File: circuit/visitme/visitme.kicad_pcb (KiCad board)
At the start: 2 copper layers, 16 parts, among them J5V1 Conn_01x01_Female, Q1 BC237

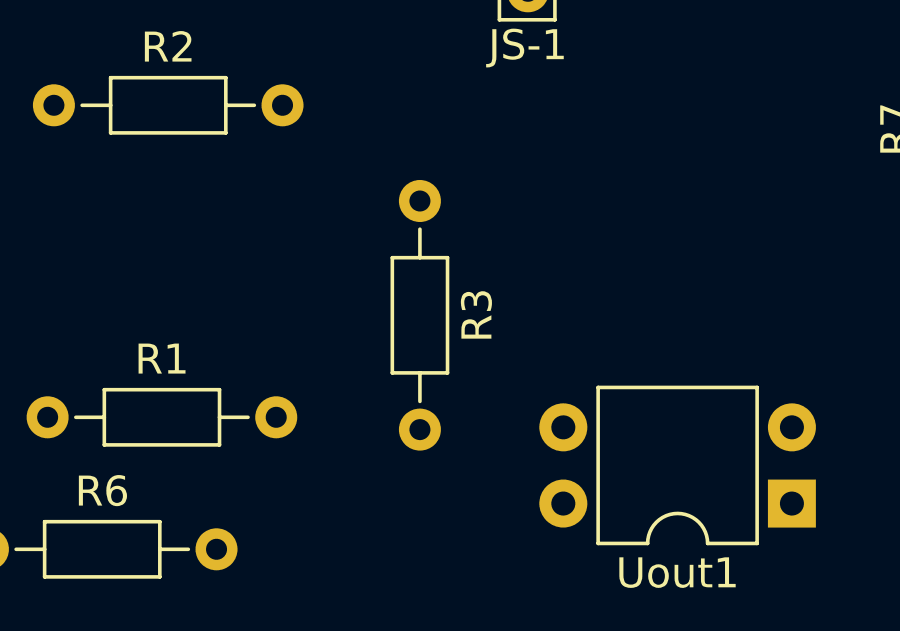
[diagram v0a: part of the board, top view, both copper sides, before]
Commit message: removed redundant 470k
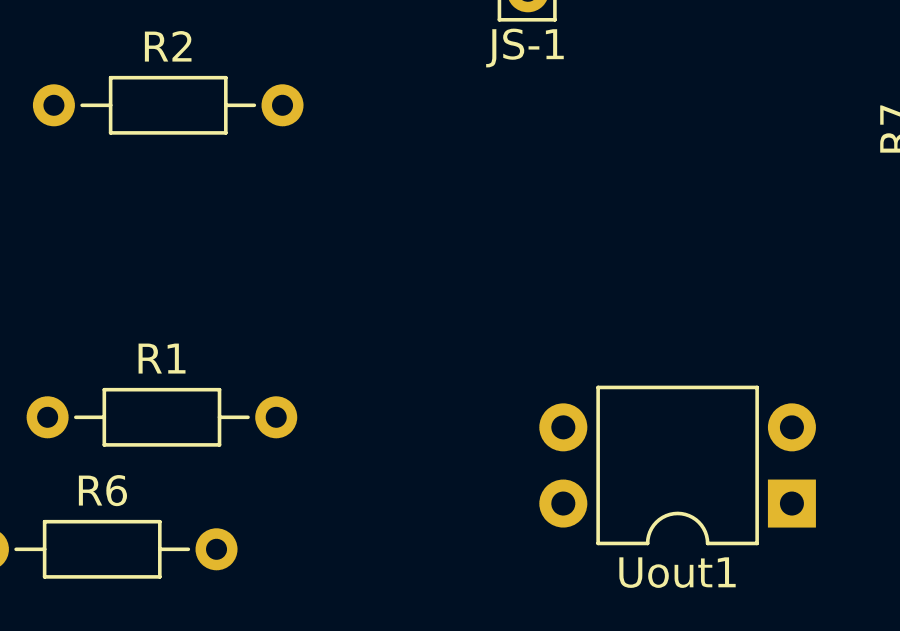
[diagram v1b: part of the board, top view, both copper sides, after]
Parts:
- removed R3: 470k, Resistor_THT:R_Axial_DIN0204_L3.6mm_D1.6mm_P7.62mm_Horizontal
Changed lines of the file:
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@@
   )
   (net 0 "")
-  (net 1 "Net-(Q1-Pad1)")
+  (net 1 "Net-(Q1-C)")
   (net 2 "D6 Data Out")
   (net 3 "+5V")
@@
     (property "Sheetfile" "visitme.kicad_sch")
     (property "Sheetname" "")
+    (property "ki_description" "Generic connector, single row, 01x01, script generated (kicad-library-utils/schlib/autogen/connector/)")
+    (property "ki_keywords" "connector")
     (attr through_hole)
     (fp_text reference "JGND1" (at 0 1.8) (layer "F.SilkS")
@@
     (property "Sheetfile" "visitme.kicad_sch")
     (property "Sheetname" "")
+    (property "ki_description" "Generic connector, single row, 01x01, script generated (kicad-library-utils/schlib/autogen/connector/)")
+    (property "ki_keywords" "connector")
     (attr through_hole)
     (fp_text reference "JS-1" (at 0 1.8) (layer "F.SilkS")
@@
     (property "Sheetfile" "visitme.kicad_sch")
     (property "Sheetname" "")
+    (property "ki_description" "Generic connector, single row, 01x01, script generated (kicad-library-utils/schlib/autogen/connector/)")
+    (property "ki_keywords" "connector")
     (attr through_hole)
     (fp_text reference "JDO1" (at 0 1.8) (layer "F.SilkS")
@@
     (property "Sheetfile" "visitme.kicad_sch")
     (property "Sheetname" "")
+    (property "ki_description" "Resistor")
+    (property "ki_keywords" "R res resistor")
     (attr through_hole)
     (fp_text reference "R4" (at 3.81 -1.92) (layer "F.SilkS")
@@
     (property "Sheetfile" "visitme.kicad_sch")
     (property "Sheetname" "")
+    (property "ki_description" "Generic connector, single row, 01x01, script generated (kicad-library-utils/schlib/autogen/connector/)")
+    (property "ki_keywords" "connector")
     (attr through_hole)
     (fp_text reference "JDI1" (at 0 1.8) (layer "F.SilkS")
@@
     (property "Sheetfile" "visitme.kicad_sch")
     (property "Sheetname" "")
+    (property "ki_description" "100mA Ic, 50V Vce, Epitaxial Silicon NPN Transistor, TO-92")
+    (property "ki_keywords" "Epitaxial Silicon NPN Transistor")
     (attr through_hole)
     (fp_text reference "Q1" (at 1.27 -3.56) (layer "F.SilkS")
@@
       (stroke (width 0.1) (type solid)) (layer "F.Fab"))
     (pad "1" thru_hole rect (at 0 0) (size 1.05 1.5) (drill 0.75) (layers "*.Cu" "*.Mask")
-      (net 1 "Net-(Q1-Pad1)") (pinfunction "C") (pintype "passive"))
+      (net 1 "Net-(Q1-C)") (pinfunction "C") (pintype "passive"))
     (pad "2" thru_hole oval (at 1.27 0) (size 1.05 1.5) (drill 0.75) (layers "*.Cu" "*.Mask")
       (net 2 "D6 Data Out") (pinfunction "B") (pintype "input"))
@@
     (property "Sheetfile" "visitme.kicad_sch")
     (property "Sheetname" "")
+    (property "ki_description" "Generic connector, single row, 01x01, script generated (kicad-library-utils/schlib/autogen/connector/)")
+    (property "ki_keywords" "connector")
     (attr through_hole)
     (fp_text reference "J5V1" (at 0 1.8) (layer "F.SilkS")
@@
     (property "Sheetfile" "visitme.kicad_sch")
     (property "Sheetname" "")
+    (property "ki_description" "Resistor")
+    (property "ki_keywords" "R res resistor")
     (attr through_hole)
     (fp_text reference "R1" (at 3.81 -1.92) (layer "F.SilkS")
@@
     (property "Sheetfile" "visitme.kicad_sch")
     (property "Sheetname" "")
+    (property "ki_description" "Resistor")
+    (property "ki_keywords" "R res resistor")
     (attr through_hole)
     (fp_text reference "R5" (at 3.81 -1.92 90) (layer "F.SilkS")
@@
     (property "Sheetfile" "visitme.kicad_sch")
     (property "Sheetname" "")
+    (property "ki_description" "Resistor")
+    (property "ki_keywords" "R res resistor")
     (attr through_hole)
     (fp_text reference "R6" (at 3.81 -1.92) (layer "F.SilkS")
@@
     (property "Sheetfile" "visitme.kicad_sch")
     (property "Sheetname" "")
+    (property "ki_description" "Generic connector, single row, 01x01, script generated (kicad-library-utils/schlib/autogen/connector/)")
+    (property "ki_keywords" "connector")
     (attr through_hole)
     (fp_text reference "JS+1" (at 0 1.8) (layer "F.SilkS")
@@
     (property "Sheetfile" "visitme.kicad_sch")
     (property "Sheetname" "")
+    (property "ki_description" "DC Optocoupler, Vce 35V, CTR 50-300%, DIP-4")
+    (property "ki_keywords" "NPN DC Optocoupler")
     (attr through_hole)
     (fp_text reference "Uout1" (at 3.81 -2.33) (layer "F.SilkS")
@@
       (stroke (width 0.1) (type solid)) (layer "F.Fab"))
     (pad "1" thru_hole rect (at 0 0 180) (size 1.6 1.6) (drill 0.8) (layers "*.Cu" "*.Mask")
-      (net 1 "Net-(Q1-Pad1)") (pintype "passive"))
+      (net 1 "Net-(Q1-C)") (pintype "passive"))
     (pad "2" thru_hole oval (at 0 2.54 180) (size 1.6 1.6) (drill 0.8) (layers "*.Cu" "*.Mask")
       (net 8 "Net-(R7-Pad1)") (pintype "passive"))
@@
     (property "Sheetfile" "visitme.kicad_sch")
     (property "Sheetname" "")
+    (property "ki_description" "Resistor")
+    (property "ki_keywords" "R res resistor")
     (attr through_hole)
     (fp_text reference "R2" (at 3.81 -1.92) (layer "F.SilkS")
@@
     )
   )
-  (footprint "Resistor_THT:R_Axial_DIN0204_L3.6mm_D1.6mm_P7.62mm_Horizontal" (layer "F.Cu")
-    (at 155.6 143.99 -90)
-    (descr "Resistor, Axial_DIN0204 series, Axial, Horizontal, pin pitch=7.62mm, 0.167W, length*diameter=3.6*1.6mm^2, http://cdn-reichelt.de/documents/datenblatt/B400/1_4W%23YAG.pdf")
-    (tags "Resistor Axial_DIN0204 series Axial Horizontal pin pitch 7.62mm 0.167W length 3.6mm diameter 1.6mm")
-    (property "Sheetfile" "visitme.kicad_sch")
-    (property "Sheetname" "")
-    (attr through_hole)
-    (fp_text reference "R3" (at 3.81 -1.92 90) (layer "F.SilkS")
-        (effects (font (size 1 1) (thickness 0.15)))
-    )
-    (fp_text value "470k" (at 3.81 1.92 90) (layer "F.Fab")
-        (effects (font (size 1 1) (thickness 0.15)))
-    )
-    (fp_text user "${REFERENCE}" (at 3.81 0 90) (layer "F.Fab")
-        (effects (font (size 0.72 0.72) (thickness 0.108)))
-    )
-    (fp_line (start 0.94 0) (end 1.89 0)
-      (stroke (width 0.12) (type solid)) (layer "F.SilkS"))
-    (fp_line (start 1.89 -0.92) (end 1.89 0.92)
-      (stroke (width 0.12) (type solid)) (layer "F.SilkS"))
-    (fp_line (start 1.89 0.92) (end 5.73 0.92)
-      (stroke (width 0.12) (type solid)) (layer "F.SilkS"))
-    (fp_line (start 5.73 -0.92) (end 1.89 -0.92)
-      (stroke (width 0.12) (type solid)) (layer "F.SilkS"))
-    (fp_line (start 5.73 0.92) (end 5.73 -0.92)
-      (stroke (width 0.12) (type solid)) (layer "F.SilkS"))
-    (fp_line (start 6.68 0) (end 5.73 0)
-      (stroke (width 0.12) (type solid)) (layer "F.SilkS"))
-    (fp_line (start -0.95 -1.05) (end -0.95 1.05)
-      (stroke (width 0.05) (type solid)) (layer "F.CrtYd"))
-    (fp_line (start -0.95 1.05) (end 8.57 1.05)
-      (stroke (width 0.05) (type solid)) (layer "F.CrtYd"))
-    (fp_line (start 8.57 -1.05) (end -0.95 -1.05)
-      (stroke (width 0.05) (type solid)) (layer "F.CrtYd"))
-    (fp_line (start 8.57 1.05) (end 8.57 -1.05)
-      (stroke (width 0.05) (type solid)) (layer "F.CrtYd"))
-    (fp_line (start 0 0) (end 2.01 0)
-      (stroke (width 0.1) (type solid)) (layer "F.Fab"))
-    (fp_line (start 2.01 -0.8) (end 2.01 0.8)
-      (stroke (width 0.1) (type solid)) (layer "F.Fab"))
-    (fp_line (start 2.01 0.8) (end 5.61 0.8)
-      (stroke (width 0.1) (type solid)) (layer "F.Fab"))
-    (fp_line (start 5.61 -0.8) (end 2.01 -0.8)
-      (stroke (width 0.1) (type solid)) (layer "F.Fab"))
-    (fp_line (start 5.61 0.8) (end 5.61 -0.8)
-      (stroke (width 0.1) (type solid)) (layer "F.Fab"))
-    (fp_line (start 7.62 0) (end 5.61 0)
-      (stroke (width 0.1) (type solid)) (layer "F.Fab"))
-    (pad "1" thru_hole circle (at 0 0 270) (size 1.4 1.4) (drill 0.7) (layers "*.Cu" "*.Mask")
-      (net 4 "Net-(R2-Pad2)") (pintype "passive"))
-    (pad "2" thru_hole oval (at 7.62 0 270) (size 1.4 1.4) (drill 0.7) (layers "*.Cu" "*.Mask")
-      (net 5 "Signal-") (pintype "passive"))
-    (model "${KICAD6_3DMODEL_DIR}/Resistor_THT.3dshapes/R_Axial_DIN0204_L3.6mm_D1.6mm_P7.62mm_Horizontal.wrl"
-      (offset (xyz 0 0 0))
-      (scale (xyz 1 1 1))
-      (rotate (xyz 0 0 0))
-    )
-  )
   (footprint "Package_DIP:DIP-4_W7.62mm" (layer "F.Cu")
     (at 160.6 128.125)
@@
     (property "Sheetfile" "visitme.kicad_sch")
     (property "Sheetname" "")
+    (property "ki_description" "DC Optocoupler, Vce 35V, CTR 50-300%, DIP-4")
+    (property "ki_keywords" "NPN DC Optocoupler")
     (attr through_hole)
     (fp_text reference "Uin1" (at 3.81 -2.33) (layer "F.SilkS")
@@
     (property "Sheetfile" "visitme.kicad_sch")
     (property "Sheetname" "")
+    (property "ki_description" "Resistor")
+    (property "ki_keywords" "R res resistor")
     (attr through_hole)
     (fp_text reference "R7" (at 3.81 -1.92 90) (layer "F.SilkS")

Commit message: further board refinement
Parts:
- moved DO 130.7 mm to (72.1, 88.1)
- moved 5V 129.4 mm to (72.0, 86.1), turned to 180 degrees
- moved Q1 128.6 mm to (67.5, 88.4), turned to -135 degrees
- moved GND 117.1 mm to (74.0, 86.1), turned to 180 degrees
- moved R4 110.9 mm to (72.9, 91.8), turned to -130 degrees
- moved DI 108.4 mm to (74.0, 88.1)
- moved S- 103.2 mm to (65.1, 94.5), turned to 90 degrees
- moved R7 102.7 mm to (85.7, 91.9), turned to 180 degrees
- moved Uout1 99.5 mm to (88.3, 94.5), turned to -90 degrees
- moved R1 90.9 mm to (65.1, 104.7), turned to 90 degrees
- moved Uin1 88.9 mm to (75.6, 102.1), turned to 90 degrees
- moved R2 83.7 mm to (68.0, 104.6)
- moved R6 79.5 mm to (78.1, 107.2)
- moved R5 77.4 mm to (68.0, 107.2), turned to 0 degrees
- moved S+ 68.7 mm to (65.1, 107.2), turned to 90 degrees
- renumbered J5V1 to 5V, JDI1 to DI, JDO1 to DO, JGND1 to GND, JS+1 to S+, JS-1 to S-
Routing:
- net Net-(Q1-C): track 0.00 -> 26.7 mm
- net Signal-: track 0.00 -> 25.3 mm
- net +5V: track 0.00 -> 18.1 mm
- net D2 Data In: track 0.00 -> 14.2 mm
- net GND: track 0.00 -> 10.1 mm
- net Signal+: track 0.00 -> 7.96 mm
- net D6 Data Out: track 0.00 -> 7.93 mm
- net Net-(R6-Pad2): track 0.00 -> 6.13 mm
- net Net-(R7-Pad1): track 0.00 -> 2.54 mm
- net Net-(R5-Pad2): track 0.00 -> 2.54 mm
- net Net-(R2-Pad2): track 0.00 -> 2.54 mm
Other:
- board outline added: 30.5 x 34 mm
